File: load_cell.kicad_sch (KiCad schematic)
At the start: 1 part, among them U7 HX711

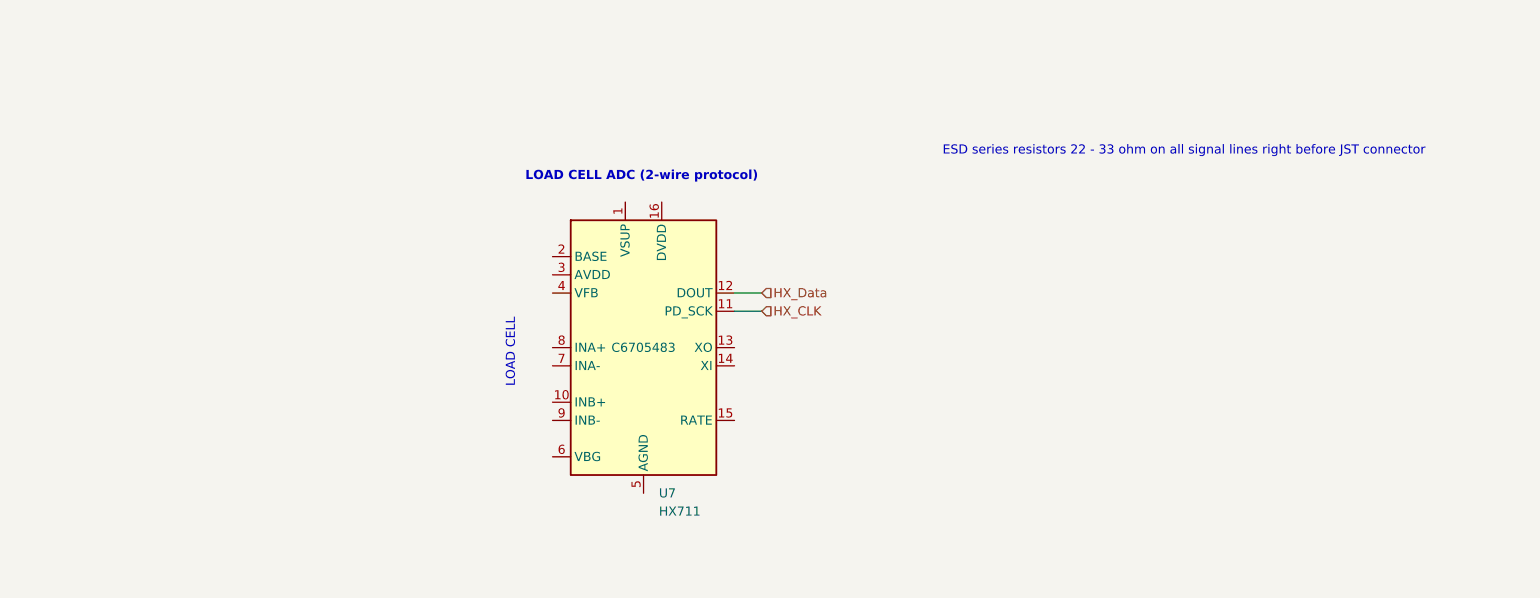
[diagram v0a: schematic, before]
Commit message: added most circuit to HX711 sch
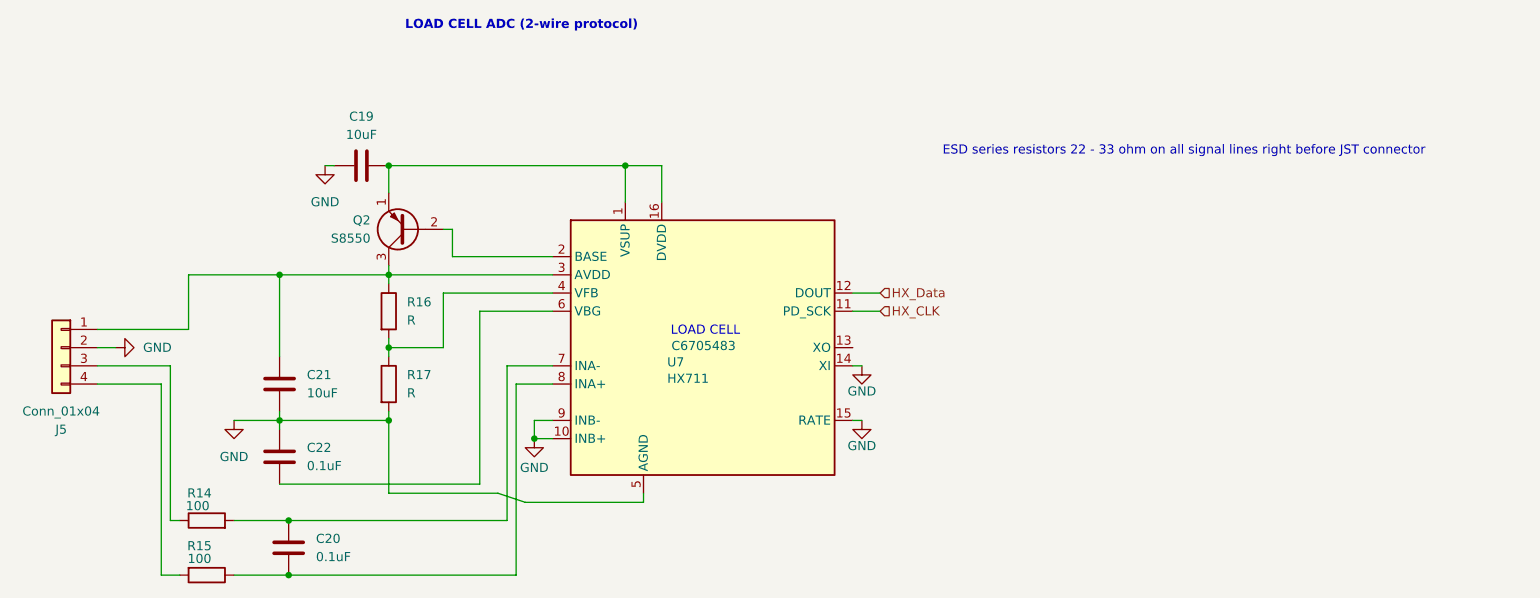
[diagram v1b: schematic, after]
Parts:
- added C19, C21: 10uF, symbol Device:C
- added C20, C22: 0.1uF, symbol Device:C
- added J5: Conn_01x04, symbol Connector_Generic:Conn_01x04
- added Q2: S8550, Package_TO_SOT_THT:TO-92_Inline, symbol Transistor_BJT:S8550
- added R14, R15: 100, symbol Device:R
- added R16, R17: R, symbol Device:R
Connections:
- net at U7.1 (VSUP): now also U7.16 (DVDD), C19.2, Q2.1 (E)
- net GND: now reaches U7.10 (INB+)
- net GND: now also U7.14 (XI), U7.15 (RATE), U7.5 (AGND), U7.9 (INB-), C19.1, C21.2, C22.1, J5.2 (Pin_2), R17.2
- net at U7.2 (BASE): now also Q2.2 (B)
- net at U7.3 (AVDD): now also C21.1, J5.1 (Pin_1), Q2.3 (C), R16.1
- net at U7.4 (VFB): now also R16.2, R17.1
- net at U7.6 (VBG): now also C22.2
- net at U7.7 (INA-): now also C20.1, R14.2
- net at U7.8 (INA+): now also C20.2, R15.1
- new net: J5.4 (Pin_4), R15.2
- new net: J5.3 (Pin_3), R14.1
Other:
- moved on the sheet: U7

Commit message: Finished HX711
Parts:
- removed J5: Conn_01x04, symbol Connector_Generic:Conn_01x04
- R16: value R -> 15k
- R17: value R -> 10k
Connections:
- net GND: now also C22.2; no longer C22.1
- net +3.3V: now reaches C19.2, Q2.1 (E), U7.1 (VSUP), U7.16 (DVDD)
- net at U7.6 (VBG): now also C22.1; no longer C22.2
- no-connect marks 0 -> 1
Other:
- note added: "E+ E- S- S+"
- moved on the sheet: C21, C22
